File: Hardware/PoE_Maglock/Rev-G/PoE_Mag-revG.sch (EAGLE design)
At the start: 84 parts, among them IC2 ATMEGA32U4-MU, J2 1X2-3.5MM, J3 1X2-3.5MM, J4 1X2-3.5MM, J5 1X2-3.5MM, J6 10103594-0001LF, Q1 35A/25V/8.5mΩ, Q3 35A/25V/8.5mΩ, Q5 35A/25V/8.5mΩ, Q6 35A/25V/8.5mΩ, SW1 SPST_TACT-KMR2, U4 W5500, X2 J1011FHY931147C, Y4 8MHz

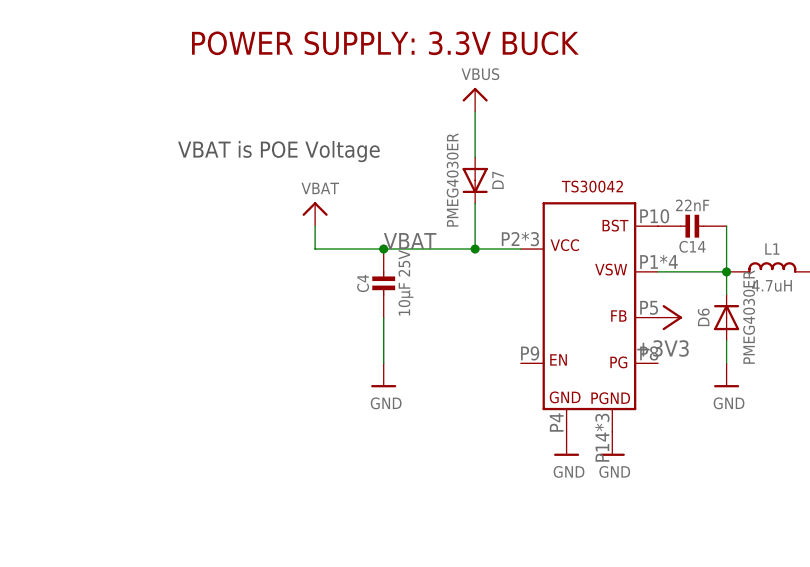
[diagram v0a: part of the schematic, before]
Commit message: HEEP-1046 added terminal blocks to schematic
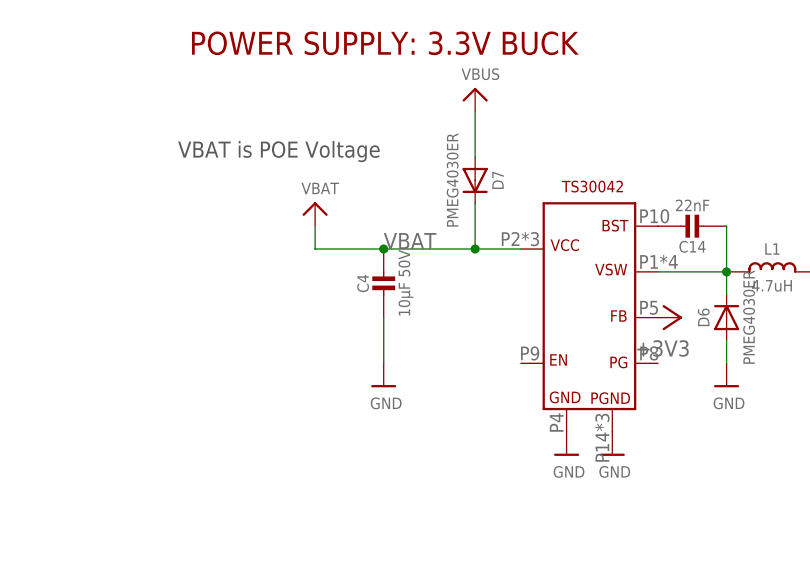
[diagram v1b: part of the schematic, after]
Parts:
- C4: value 10µF 25V -> 10µF 50V; device microbuilder:CAP_CERAMIC0603MINI -> microbuilder:CAP_CERAMIC_0805
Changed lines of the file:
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@@
 <?xml version="1.0" encoding="utf-8"?>
 <!DOCTYPE eagle SYSTEM "eagle.dtd">
-<eagle version="8.6.3">
+<eagle version="9.0.1">
 <drawing>
 <settings>
@@
 <grid distance="0.1" unitdist="inch" unit="inch" style="lines" multiple="1" display="no" altdistance="0.01" altunitdist="inch" altunit="inch"/>
 <layers>
-<layer number="1" name="Top" color="4" fill="1" visible="no" active="no"/>
-<layer number="16" name="Bottom" color="1" fill="1" visible="no" active="no"/>
-<layer number="17" name="Pads" color="2" fill="1" visible="no" active="no"/>
-<layer number="18" name="Vias" color="2" fill="1" visible="no" active="no"/>
-<layer number="19" name="Unrouted" color="6" fill="1" visible="no" active="no"/>
-<layer number="20" name="Dimension" color="24" fill="1" visible="no" active="no"/>
-<layer number="21" name="tPlace" color="7" fill="1" visible="no" active="no"/>
-<layer number="22" name="bPlace" color="7" fill="1" visible="no" active="no"/>
-<layer number="23" name="tOrigins" color="15" fill="1" visible="no" active="no"/>
-<layer number="24" name="bOrigins" color="15" fill="1" visible="no" active="no"/>
-<layer number="25" name="tNames" color="7" fill="1" visible="no" active="no"/>
-<layer number="26" name="bNames" color="7" fill="1" visible="no" active="no"/>
-<layer number="27" name="tValues" color="9" fill="1" visible="no" active="no"/>
-<layer number="28" name="bValues" color="7" fill="1" visible="no" active="no"/>
+<layer number="1" name="Top" color="4" fill="1" visible="yes" active="no"/>
+<layer number="16" name="Bottom" color="1" fill="1" visible="yes" active="no"/>
+<layer number="17" name="Pads" color="2" fill="1" visible="yes" active="no"/>
+<layer number="18" name="Vias" color="2" fill="1" visible="yes" active="no"/>
+<layer number="19" name="Unrouted" color="15" fill="1" visible="yes" active="no"/>
+<layer number="20" name="Dimension" color="24" fill="1" visible="yes" active="no"/>
+<layer number="21" name="tPlace" color="14" fill="1" visible="yes" active="no"/>
+<layer number="22" name="bPlace" color="7" fill="1" visible="yes" active="no"/>
+<layer number="23" name="tOrigins" color="15" fill="1" visible="yes" active="no"/>
+<layer number="24" name="bOrigins" color="15" fill="1" visible="yes" active="no"/>
+<layer number="25" name="tNames" color="7" fill="1" visible="yes" active="no"/>
+<layer number="26" name="bNames" color="7" fill="1" visible="yes" active="no"/>
+<layer number="27" name="tValues" color="15" fill="1" visible="yes" active="no"/>
+<layer number="28" name="bValues" color="7" fill="1" visible="yes" active="no"/>
 <layer number="29" name="tStop" color="7" fill="3" visible="no" active="no"/>
 <layer number="30" name="bStop" color="7" fill="6" visible="no" active="no"/>
@@
 <layer number="35" name="tGlue" color="7" fill="4" visible="no" active="no"/>
 <layer number="36" name="bGlue" color="7" fill="5" visible="no" active="no"/>
-<layer number="37" name="tTest" color="7" fill="1" visible="no" active="no"/>
-<layer number="38" name="bTest" color="7" fill="1" visible="no" active="no"/>
+<layer number="37" name="tTest" color="7" fill="1" visible="yes" active="no"/>
+<layer number="38" name="bTest" color="7" fill="1" visible="yes" active="no"/>
 <layer number="39" name="tKeepout" color="4" fill="11" visible="no" active="no"/>
 <layer number="40" name="bKeepout" color="1" fill="11" visible="no" active="no"/>
@@
 <layer number="44" name="Drills" color="7" fill="1" visible="no" active="no"/>
 <layer number="45" name="Holes" color="7" fill="1" visible="no" active="no"/>
-<layer number="46" name="Milling" color="3" fill="1" visible="no" active="no"/>
-<layer number="47" name="Measures" color="7" fill="1" visible="no" active="no"/>
-<layer number="48" name="Document" color="7" fill="1" visible="no" active="no"/>
-<layer number="49" name="Reference" color="7" fill="1" visible="no" active="no"/>
-<layer number="50" name="dxf" color="7" fill="1" visible="no" active="no"/>
-<layer number="51" name="tDocu" color="7" fill="1" visible="no" active="no"/>
-<layer number="52" name="bDocu" color="7" fill="1" visible="no" active="no"/>
-<layer number="53" name="tGND_GNDA" color="7" fill="9" visible="no" active="no"/>
-<layer number="54" name="bGND_GNDA" color="1" fill="9" visible="no" active="no"/>
-<layer number="56" name="wert" color="7" fill="1" visible="no" active="no"/>
-<layer number="57" name="tCAD" color="7" fill="1" visible="no" active="no"/>
-<layer number="59" name="tCarbon" color="7" fill="1" visible="no" active="no"/>
-<layer number="60" name="bCarbon" color="7" fill="1" visible="no" active="no"/>
+<layer number="46" name="Milling" color="3" fill="1" visible="yes" active="no"/>
+<layer number="47" name="Measures" color="7" fill="1" visible="yes" active="no"/>
+<layer number="48" name="Document" color="7" fill="1" visible="yes" active="no"/>
+<layer number="49" name="Reference" color="7" fill="1" visible="yes" active="no"/>
+<layer number="50" name="dxf" color="7" fill="1" visible="yes" active="no"/>
+<layer number="51" name="tDocu" color="7" fill="1" visible="yes" active="no"/>
+<layer number="52" name="bDocu" color="7" fill="1" visible="yes" active="no"/>
+<layer number="53" name="tGND_GNDA" color="7" fill="9" visible="yes" active="no"/>
+<layer number="54" name="bGND_GNDA" color="1" fill="9" visible="yes" active="no"/>
+<layer number="56" name="wert" color="7" fill="1" visible="yes" active="no"/>
+<layer number="57" name="tCAD" color="7" fill="1" visible="yes" active="no"/>
+<layer number="59" name="tCarbon" color="7" fill="1" visible="yes" active="no"/>
+<layer number="60" name="bCarbon" color="7" fill="1" visible="yes" active="no"/>
 <layer number="90" name="Modules" color="5" fill="1" visible="yes" active="yes"/>
 <layer number="91" name="Nets" color="2" fill="1" visible="yes" active="yes"/>
@@
 <part name="+3V5" library="supply1" deviceset="+3V3" device=""/>
 <part name="U$19" library="Heep" deviceset="BUCK_CONVERTER" device=""/>
-<part name="C4" library="microbuilder" deviceset="CAP_CERAMIC" device="0603MINI" value="10µF 25V"/>
+<part name="C4" library="microbuilder" deviceset="CAP_CERAMIC" device="_0805" value="10µF 50V"/>
 <part name="U$20" library="microbuilder" deviceset="GND" device=""/>
 <part name="U$22" library="microbuilder" deviceset="GND" device=""/>

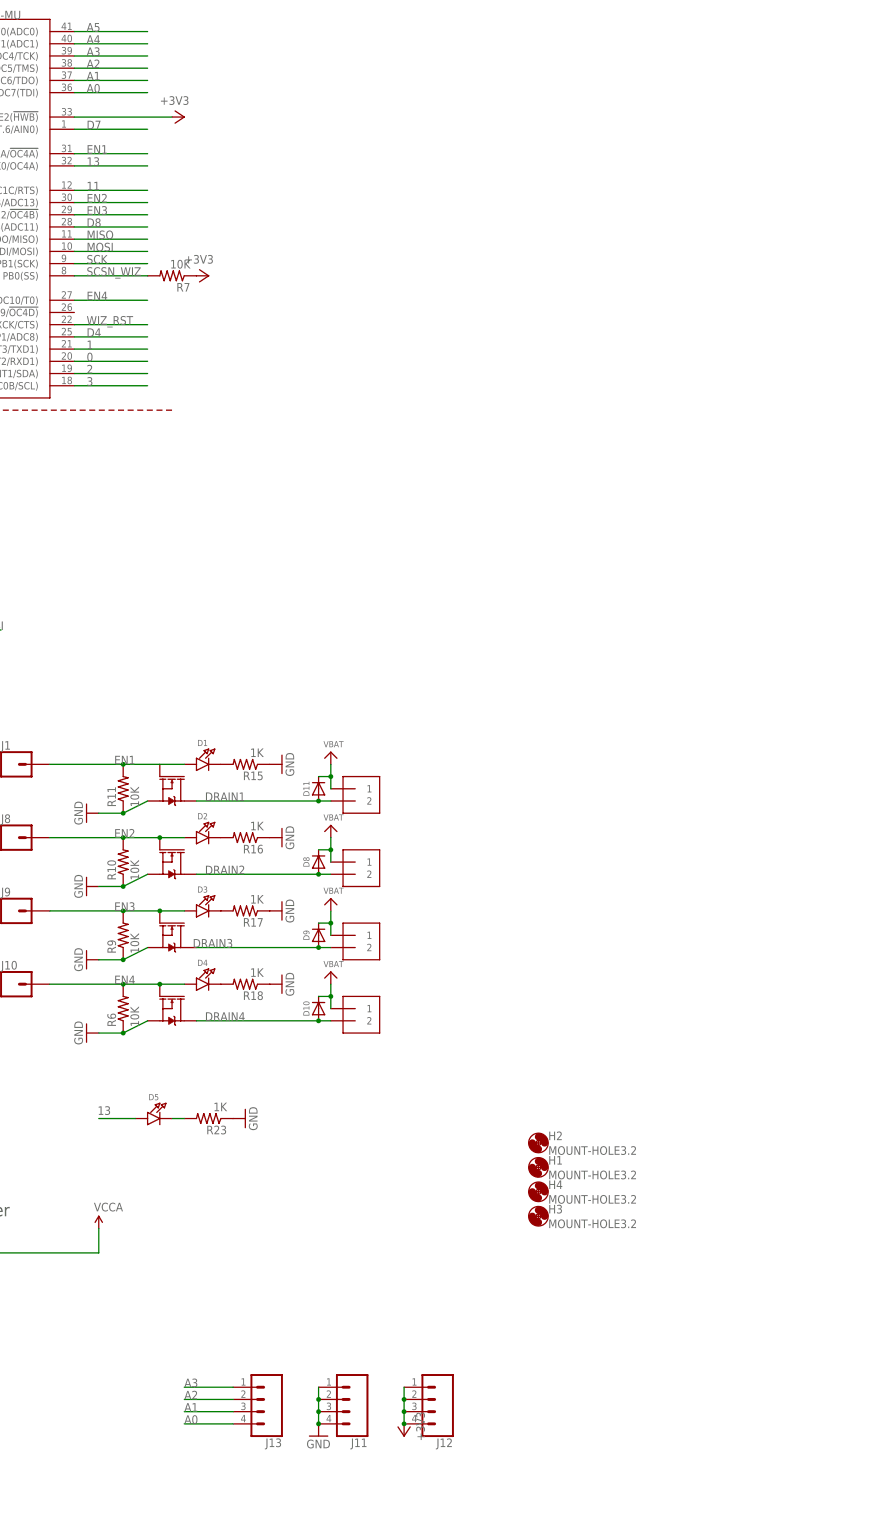
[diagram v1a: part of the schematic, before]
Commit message: HEEP-1046 added analog terminal blocks to schematic
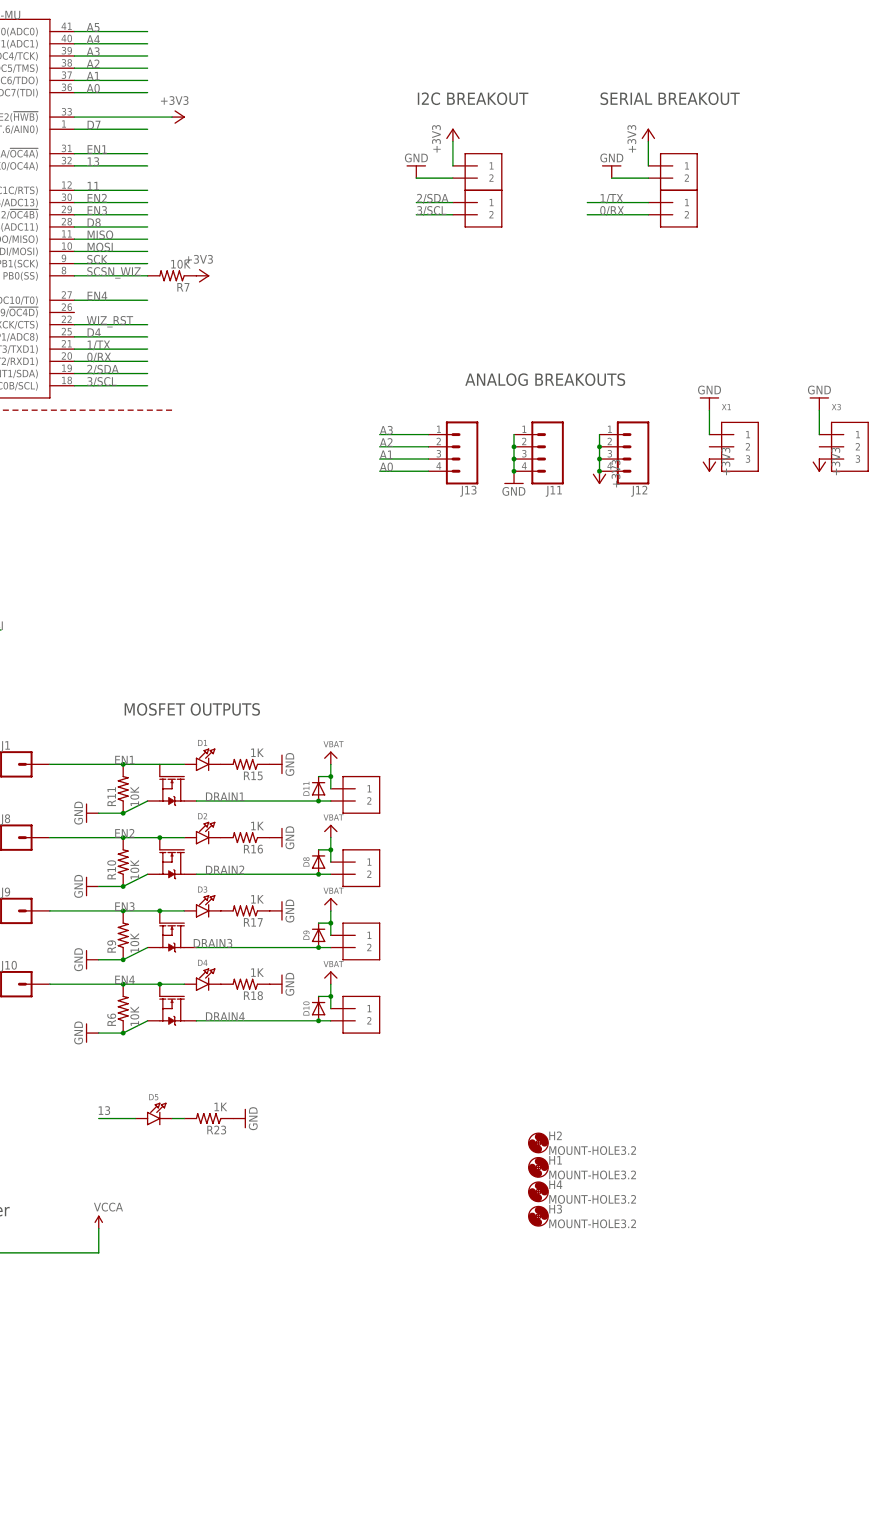
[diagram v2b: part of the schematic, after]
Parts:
- added J14, J15, J16, J17: 1X2-3.5MM, adafruit:1X2-3.5MM
- added X1, X3: (no value), microbuilder:TERMBLOCK_1X3
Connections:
- removed net 0: IC2.PD2(INT2/RXD1)
- removed net 1: IC2.PD3(INT3/TXD1)
- removed net 2: IC2.PD1(INT1/SDA)
- removed net 3: IC2.PD0(INT0/OC0B/SCL)
- new net 0/RX: IC2.PD2(INT2/RXD1), J17.2
- new net 1/TX: IC2.PD3(INT3/TXD1), J17.1
- new net 2/SDA: IC2.PD1(INT1/SDA), J15.1
- new net 3/SCL: IC2.PD0(INT0/OC0B/SCL), J15.2
- net +3V3: now also J14.1, J16.1, X1.3, X3.3
- net GND: now also J14.2, J16.2, X1.1, X3.1
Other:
- note added: "ANALOG BREAKOUTS"
- note added: "I2C BREAKOUT"
- note added: "MOSFET OUTPUTS"
- note added: "SERIAL BREAKOUT"
- moved on the sheet: J11, J12, J13

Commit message: HEEP-1046 added DC jack to schematic and to brd. not yet positioned
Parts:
- removed J11, J12: (no value), SparkFun-Connectors:CONN_04
- removed J13: (no value), SparkFun-Connectors:CONN_041X04_NO_SILK
- added D12: PMEG4030ER, microbuilder:DIODESOD-123
- added U$4: 2.1MMJACKTHM, adafruit:2.1MMJACKTHM
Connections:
- new net N$1: D12.A, U$4.TIP
- net +3V3: no longer J12.1, J12.2, J12.3, J12.4
- net A0: no longer J13.4
- net A1: no longer J13.3
- net A2: no longer J13.2
- net A3: no longer J13.1
- net GND: now also U$4.RING, U$4.RING_SW; no longer J11.1, J11.2, J11.3, J11.4
- net VBAT: now also D12.C
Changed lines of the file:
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@@
 <part name="J9" library="SparkFun-Connectors" deviceset="CONN_01" device=""/>
 <part name="J10" library="SparkFun-Connectors" deviceset="CONN_01" device=""/>
-<part name="J11" library="SparkFun-Connectors" deviceset="CONN_04" device=""/>
-<part name="J12" library="SparkFun-Connectors" deviceset="CONN_04" device=""/>
-<part name="J13" library="SparkFun-Connectors" deviceset="CONN_04" device="1X04_NO_SILK"/>
-<part name="GND10" library="supply1" deviceset="GND" device=""/>
-<part name="+3V13" library="supply1" deviceset="+3V3" device=""/>
 <part name="+3V11" library="supply1" deviceset="+3V3" device=""/>
 <part name="+3V4" library="supply1" deviceset="+3V3" device=""/>
@@
 <part name="+3V14" library="supply1" deviceset="+3V3" device=""/>
 <part name="+3V15" library="supply1" deviceset="+3V3" device=""/>
+<part name="U$4" library="adafruit" library_urn="urn:adsk.eagle:library:420" deviceset="2.1MMJACK" device="THM"/>
+<part name="U$17" library="microbuilder" deviceset="GND" device=""/>
+<part name="D12" library="microbuilder" deviceset="DIODE" device="SOD-123" value="PMEG4030ER"/>
+<part name="U$16" library="microbuilder" deviceset="VBAT" device=""/>
 </parts>
 <sheets>
@@
 <instance part="J9" gate="G$1" x="276.86" y="149.86"/>
 <instance part="J10" gate="G$1" x="276.86" y="134.62"/>
-<instance part="J11" gate="G$1" x="386.08" y="246.38" rot="R180"/>
-<instance part="J12" gate="G$1" x="403.86" y="246.38" rot="R180"/>
-<instance part="J13" gate="G$1" x="368.3" y="246.38" rot="R180"/>
-<instance part="GND10" gate="1" x="381" y="238.76"/>
-<instance part="+3V13" gate="G$1" x="398.78" y="238.76" rot="R180"/>
 <instance part="+3V11" gate="G$1" x="152.4" y="226.06" rot="MR90"/>
 <instance part="+3V4" gate="G$1" x="116.84" y="220.98" rot="MR90"/>
@@
 <instance part="+3V14" gate="G$1" x="444.5" y="241.3" rot="R180"/>
 <instance part="+3V15" gate="G$1" x="421.64" y="241.3" rot="R180"/>
+<instance part="U$4" gate="G$1" x="38.1" y="223.52"/>
+<instance part="U$17" gate="G$1" x="43.18" y="218.44"/>
+<instance part="D12" gate="G$1" x="53.34" y="226.06"/>
+<instance part="U$16" gate="G$1" x="66.04" y="226.06" rot="R270"/>
 </instances>
 <busses>
@@
 </segment>
 <segment>
-<pinref part="J11" gate="G$1" pin="4"/>
-<pinref part="GND10" gate="1" pin="GND"/>
-<pinref part="J11" gate="G$1" pin="3"/>
-<wire x1="381" y1="241.3" x2="381" y2="243.84" width="0.1524" layer="91"/>
-<junction x="381" y="241.3"/>
-<pinref part="J11" gate="G$1" pin="2"/>
-<wire x1="381" y1="243.84" x2="381" y2="246.38" width="0.1524" layer="91"/>
-<junction x="381" y="243.84"/>
-<pinref part="J11" gate="G$1" pin="1"/>
-<wire x1="381" y1="246.38" x2="381" y2="248.92" width="0.1524" layer="91"/>
-<junction x="381" y="246.38"/>
-</segment>
-<segment>
 <pinref part="D6" gate="G$1" pin="A"/>
 <pinref part="U$11" gate="G$1" pin="GND"/>
@@
 <pinref part="GND31" gate="1" pin="GND"/>
 <wire x1="444.5" y1="254" x2="444.5" y2="248.92" width="0.1524" layer="91"/>
+</segment>
+<segment>
+<pinref part="U$4" gate="G$1" pin="RING"/>
+<pinref part="U$17" gate="G$1" pin="GND"/>
+<pinref part="U$4" gate="G$1" pin="RING_SW"/>
+<wire x1="43.18" y1="223.52" x2="43.18" y2="220.98" width="0.1524" layer="91"/>
+<junction x="43.18" y="220.98"/>
 </segment>
 </net>
@@
 </segment>
 <segment>
-<pinref part="J13" gate="G$1" pin="1"/>
 <wire x1="363.22" y1="248.92" x2="353.06" y2="248.92" width="0.1524" layer="91"/>
 <label x="353.06" y="248.92" size="1.778" layer="95"/>
@@
 </segment>
 <segment>
-<pinref part="J13" gate="G$1" pin="2"/>
 <wire x1="363.22" y1="246.38" x2="353.06" y2="246.38" width="0.1524" layer="91"/>
 <label x="353.06" y="246.38" size="1.778" layer="95"/>
@@
 </segment>
 <segment>
-<pinref part="J13" gate="G$1" pin="3"/>
 <wire x1="363.22" y1="243.84" x2="353.06" y2="243.84" width="0.1524" layer="91"/>
 <label x="353.06" y="243.84" size="1.778" layer="95"/>
@@
 </segment>
 <segment>
-<pinref part="J12" gate="G$1" pin="4"/>
-<pinref part="+3V13" gate="G$1" pin="+3V3"/>
-<pinref part="J12" gate="G$1" pin="1"/>
-<pinref part="J12" gate="G$1" pin="2"/>
-<wire x1="398.78" y1="248.92" x2="398.78" y2="246.38" width="0.1524" layer="91"/>
-<pinref part="J12" gate="G$1" pin="3"/>
-<wire x1="398.78" y1="246.38" x2="398.78" y2="243.84" width="0.1524" layer="91"/>
-<junction x="398.78" y="246.38"/>
-<wire x1="398.78" y1="243.84" x2="398.78" y2="241.3" width="0.1524" layer="91"/>
-<junction x="398.78" y="243.84"/>
-<junction x="398.78" y="241.3"/>
-</segment>
-<segment>
 <pinref part="L1" gate="G$1" pin="2"/>
 <pinref part="C12" gate="G$1" pin="1"/>
@@
 <wire x1="363.22" y1="241.3" x2="353.06" y2="241.3" width="0.1524" layer="91"/>
 <label x="353.06" y="241.3" size="1.778" layer="95"/>
-<pinref part="J13" gate="G$1" pin="4"/>
 </segment>
 </net>
@@
 <pinref part="U$1" gate="G$1" pin="VBAT"/>
 </segment>
+<segment>
+<pinref part="D12" gate="G$1" pin="C"/>
+<wire x1="55.88" y1="226.06" x2="63.5" y2="226.06" width="0.1524" layer="91"/>
+<pinref part="U$16" gate="G$1" pin="VBAT"/>
+</segment>
 </net>
 <net name="N$5" class="0">
@@
 </segment>
 </net>
+<net name="N$1" class="0">
+<segment>
+<pinref part="U$4" gate="G$1" pin="TIP"/>
+<pinref part="D12" gate="G$1" pin="A"/>
+<wire x1="43.18" y1="226.06" x2="50.8" y2="226.06" width="0.1524" layer="91"/>
+</segment>
+</net>
